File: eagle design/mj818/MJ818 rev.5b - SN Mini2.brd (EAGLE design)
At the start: 35.5 x 35.5 mm, 42 parts, among them IC202 LDK320AM33R, IC302 STM32F042G6U6, IC401 TCAN334, IC506 MAX16820, IC507 SQA470EEJ-T1_GE3, IC601 MAX16839

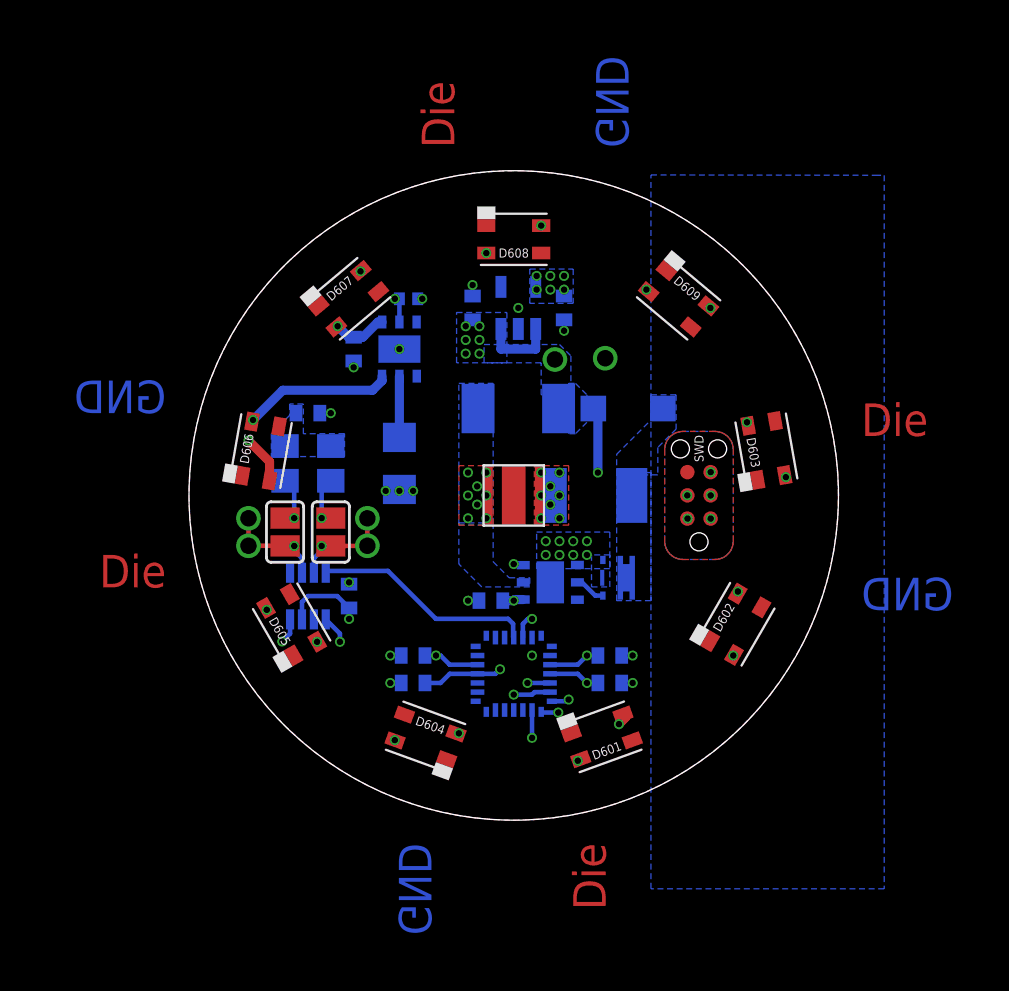
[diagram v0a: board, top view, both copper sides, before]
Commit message: /// start of MJ818 rev.5b - SN Mini2 /// - added CAN protection diode - added power supervisor - replaced CAN solder bridges with 0402 resistors - adapted silkscreen stuff a bit - deleted old original mj818 MagicShine board/schematic - renamed files, updated HW rev. in sch & brd
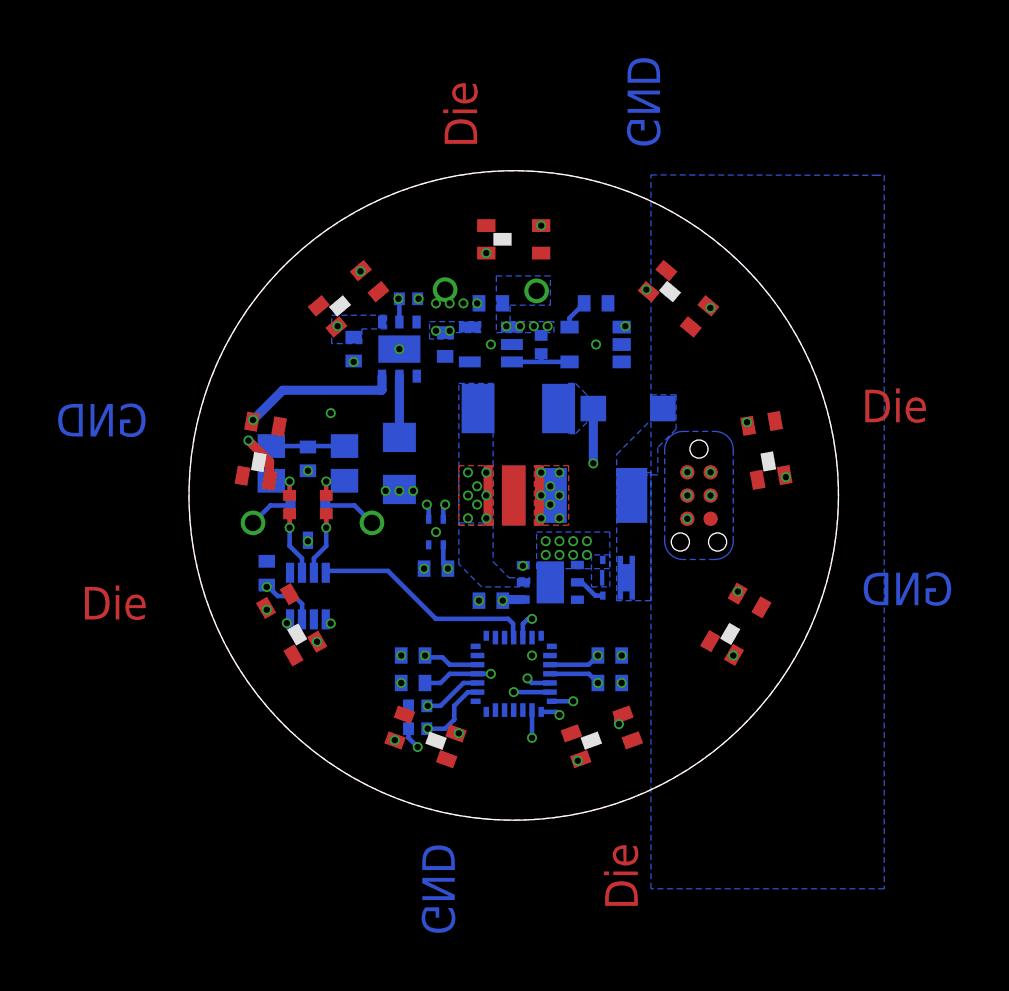
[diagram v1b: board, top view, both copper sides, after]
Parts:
- removed SJ401: CAN H term., jumper:SJ
- removed SJ402: CAN L term., jumper:SJ
- removed TP1: CAN high, signal testpoint:TH-0.9
- removed TP2: CAN low, signal testpoint:TH-0.9
- added C201: 1uF / 10V, rcl:C0402
- added C705: 0.1uF / 10V, rcl:C0402
- added IC201: R3119N058A, R3119x - Input Voltage Detector:SOT23-5
- added IC402: SZNUP2105LT1G, NUP2105L - 27V ESD Protection Diode:SOT-23-3
- added IC701: SHT40-AD1F-R2, SHT40-AD1F - Humidity Sensor:SMD
- added R201: 100k / 0.1W, rcl:R0402
- added R301, R302: 2k2, rcl:R0402
- added R403, R404: 0, rcl:R0402
- moved TP102 9.52 mm to (-3.75, 11.2)
- moved C207 6.80 mm to (-3.75, 8.25)
- moved SWD1 5.07 mm to (10.1, 2.54), turned to 270 degrees
- moved C405 4.67 mm to (-13.5, -4.25)
- moved TP101 3.88 mm to (1.25, 11.2)
- moved C401 2.50 mm to (-11.2, 2.00), turned to 270 degrees
- moved IC202 2.50 mm to (-1.25, 8.25), turned to 90 degrees
- moved TP105 1.27 mm to (-7.75, -1.50)
- moved TP106 1.27 mm to (-14.2, -1.50)
- moved C202 1.03 mm to (-1.25, 10.5), turned to 0 degrees
- moved R401 0.75 mm to (-13.2, 1.75)
- moved R402 0.75 mm to (-9.25, 1.75)
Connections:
- new net I2C_SCL: IC302.3_PF1, IC701.SCL, R302.1
- new net I2C_SDA: IC302.2_PF0, IC701.SDA, R301.1
- new net POWER_3V3:CD: C201.1, IC201.5_CD
- new net POWER_3V3:EN: IC201.4_DOUT, IC202.EN, R201.2
- net 3V3: now also C705.1, IC701.VDD, R301.2, R302.2
- net BAT+: now also IC201.1_VDD, R201.1; no longer IC202.EN
- net CAN_H: now also IC402.2, R403.2; no longer SJ401.1, TP1.P$1
- net CAN_INFRA:H: now also R403.1; no longer SJ401.2
- net CAN_INFRA:L: now also R404.1; no longer SJ402.2
- net CAN_L: now also IC402.1, R404.2; no longer SJ402.1, TP2.P$1
- net GND: now also C201.2, C705.2, IC201.2_GND, IC201.3_GND, IC402.3, IC701.VSS
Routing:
- net BAT+: track 46.0 -> 4.80 mm, vias 11 -> 10
- net I2C_SDA: track 0.00 -> 20.5 mm, vias 0 -> 2
- net I2C_SCL: track 0.00 -> 18.3 mm, vias 0 -> 2
- net SYS_SWDIO: track 13.6 -> 18.0 mm
- net CAN_INFRA:SPLIT: track 0.00 -> 4.07 mm
- net POWER_3V3:EN: track 0.00 -> 3.60 mm
- net SYS_SWCLK: track 20.0 -> 23.3 mm
- net REAR_LED_DRIVER:SINK: track 43.9 -> 46.6 mm
- net 3V3: track 13.6 -> 15.9 mm, vias 11 -> 9
- net CAN_H: track 5.64 -> 7.68 mm
- net REAR_LED_DRIVER:D5,D6: track 12.7 -> 14.4 mm
- net POWER_3V3:CD: track 0.00 -> 1.63 mm
- net CAN_L: track 5.64 -> 7.18 mm
- net REAR_LED_DRIVER:D4,D5: track 6.89 -> 7.90 mm
- net CAN_INFRA:L: track 2.75 -> 1.78 mm
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- added copper zone on layer 2, net CLEAR
- added copper zone on layer 14, net GND
- added copper zone on layer 3, net GND
- removed copper zone on layer 16, net CAN_INFRA:SPLIT
- removed copper zone on layer 1, net CUT
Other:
- board text added: "MJ818 SuperNova Mini2 ejovrh rev. 5b"
- board text removed: "CAN term."
- board text removed: "MJ818 clone SuperNova Mini2 ejovrh rev. 5a"

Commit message: in sch: - changed I2C pullup resistors to 1k
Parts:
- R301, R302: value 2k2 -> 1k
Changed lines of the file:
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@@
 <attribute name="VALUE" x="-3.615" y="-5.905" size="1.27" layer="28" rot="MR0"/>
 </element>
-<element name="R302" library="rcl" library_urn="urn:adsk.eagle:library:334" package="R0402" package3d_urn="urn:adsk.eagle:package:23547/3" value="2k2" x="-5.25" y="-11.5" smashed="yes" rot="MR0">
+<element name="R302" library="rcl" library_urn="urn:adsk.eagle:library:334" package="R0402" package3d_urn="urn:adsk.eagle:package:23547/3" value="1k" x="-5.25" y="-11.5" smashed="yes" rot="MR0">
 <attribute name="POPULARITY" value="0" x="-5.25" y="-6.5" size="1.778" layer="28" rot="MR0" display="off"/>
 <attribute name="SPICEPREFIX" value="R" x="-5.25" y="-6.5" size="1.778" layer="28" rot="MR0" display="off"/>
 <attribute name="VALUE" x="-4.615" y="-13.405" size="1.27" layer="28" rot="MR0"/>
 </element>
-<element name="R301" library="rcl" library_urn="urn:adsk.eagle:library:334" package="R0402" package3d_urn="urn:adsk.eagle:package:23547/3" value="2k2" x="-5.25" y="-12.75" smashed="yes" rot="MR0">
+<element name="R301" library="rcl" library_urn="urn:adsk.eagle:library:334" package="R0402" package3d_urn="urn:adsk.eagle:package:23547/3" value="1k" x="-5.25" y="-12.75" smashed="yes" rot="MR0">
 <attribute name="POPULARITY" value="0" x="-5.25" y="-17.75" size="1.778" layer="28" rot="MR0" display="off"/>
 <attribute name="SPICEPREFIX" value="R" x="-5.25" y="-17.75" size="1.778" layer="28" rot="MR0" display="off"/>
